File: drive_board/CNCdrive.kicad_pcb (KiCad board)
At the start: 2 copper layers, 1 part, among them U1 DRV8711

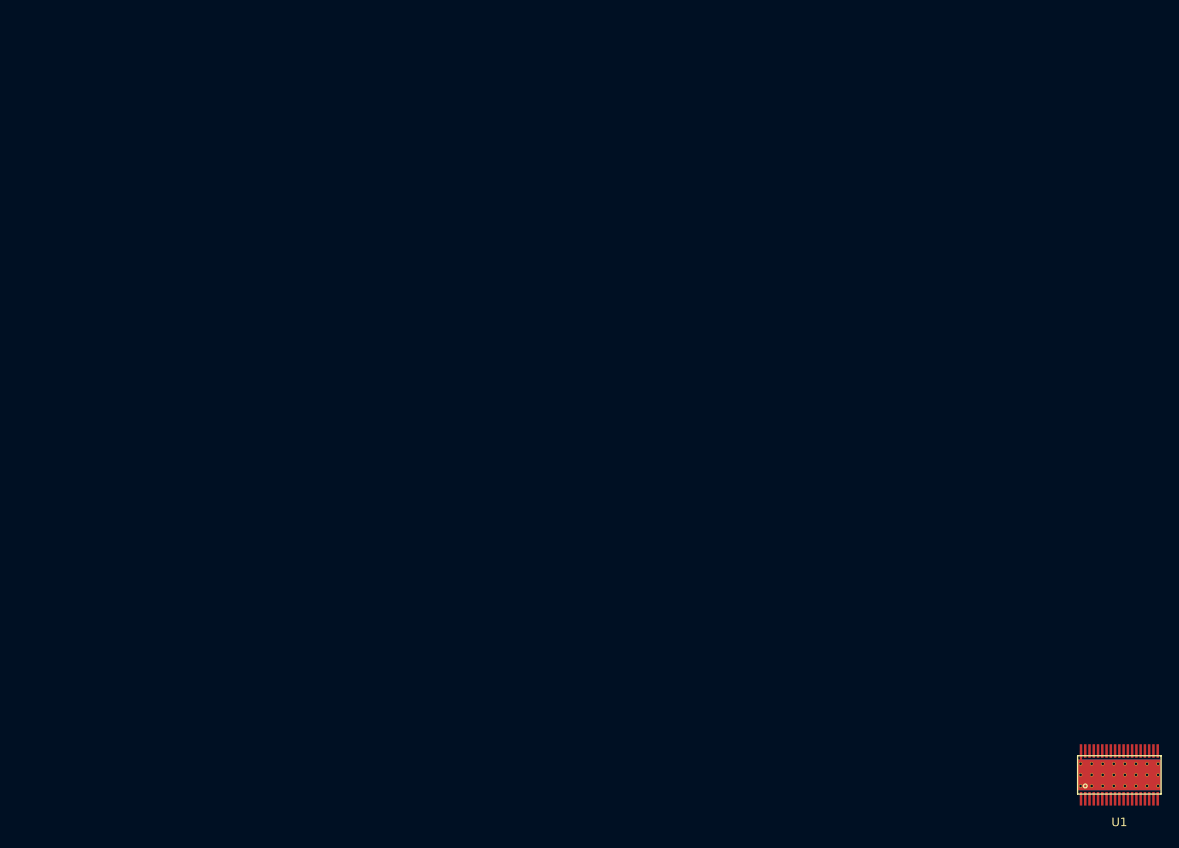
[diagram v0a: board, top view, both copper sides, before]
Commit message: associated footprints, connectors, fuse, leds might need change
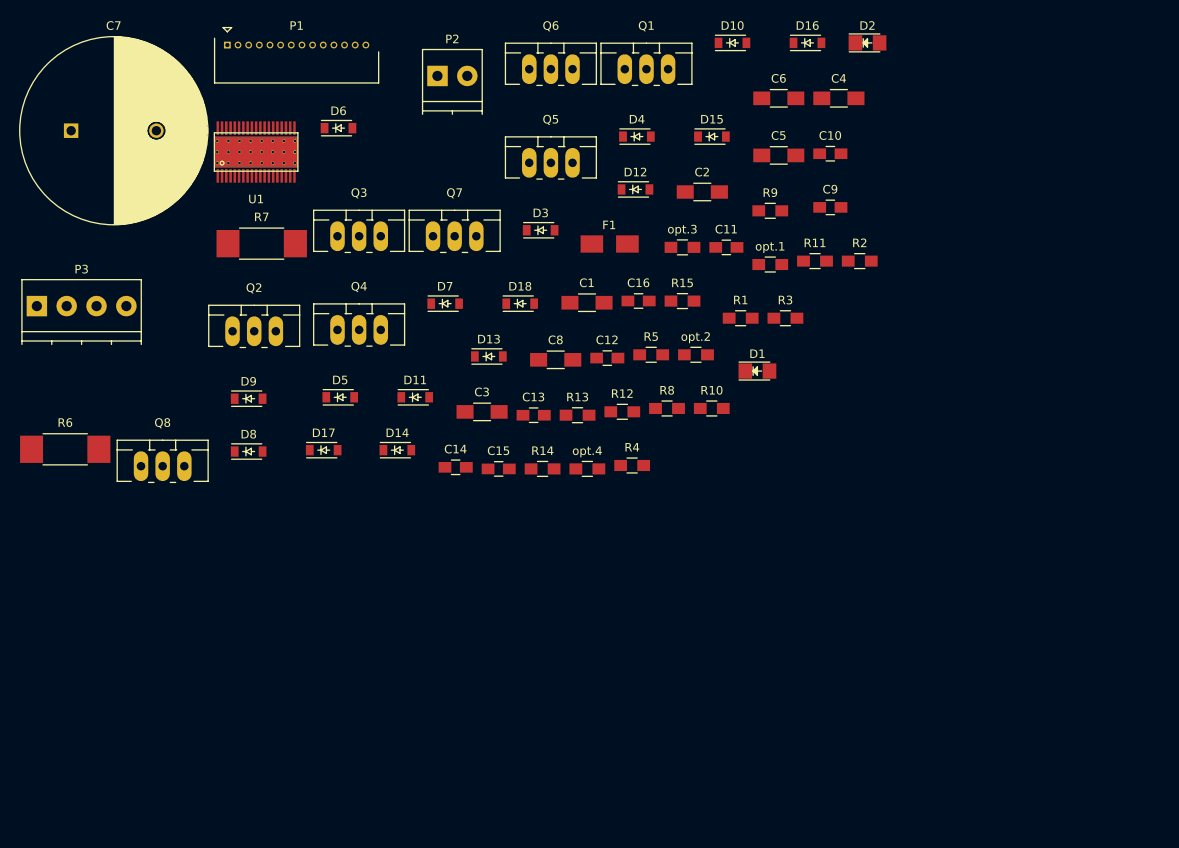
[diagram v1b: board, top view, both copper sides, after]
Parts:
- added C1: 100u, Capacitors_SMD:C_1206_HandSoldering, F.Cu at (86.0, 49.6)
- added C10: snub, Capacitors_SMD:C_0805_HandSoldering, F.Cu at (114.6, 32.1)
- added C11: snub, Capacitors_SMD:C_0805_HandSoldering, F.Cu at (102.4, 43.1)
- added C12: snub, Capacitors_SMD:C_0805_HandSoldering, F.Cu at (88.4, 56.1)
- added C13: snub, Capacitors_SMD:C_0805_HandSoldering, F.Cu at (79.8, 62.8)
- added C14: snub, Capacitors_SMD:C_0805_HandSoldering, F.Cu at (70.6, 68.9)
- added C15: snub, Capacitors_SMD:C_0805_HandSoldering, F.Cu at (75.7, 69.1)
- added C16: snub, Capacitors_SMD:C_0805_HandSoldering, F.Cu at (92.1, 49.4)
- added C2: 10n, Capacitors_SMD:C_1206_HandSoldering, F.Cu at (99.6, 36.6)
- added C3: 100n, Capacitors_SMD:C_1206_HandSoldering, F.Cu at (73.7, 62.4)
- added C4: 1u, Capacitors_SMD:C_1206_HandSoldering, F.Cu at (115.6, 25.6)
- added C5: 1u, Capacitors_SMD:C_1206_HandSoldering, F.Cu at (108.5, 32.3)
- added C6: 100n, Capacitors_SMD:C_1206_HandSoldering, F.Cu at (108.5, 25.6)
- added C7: 1000u, Capacitors_ThroughHole:C_Radial_D22_L41_P10, F.Cu at (25.5, 29.4)
- added C8: 1n, Capacitors_SMD:C_1206_HandSoldering, F.Cu at (82.4, 56.3)
- added C9: snub, Capacitors_SMD:C_0805_HandSoldering, F.Cu at (114.6, 38.4)
- added D1: LED, LEDs:LED_1206, F.Cu at (106.0, 57.6)
- added D10: ZENER opt., Diodes_SMD:SOD-123, F.Cu at (103.1, 19.1)
- added D11: D_Schottky, Diodes_SMD:SOD-123, F.Cu at (65.9, 60.7)
- added D12: D_Schottky, Diodes_SMD:SOD-123, F.Cu at (91.7, 36.3)
- added D13: D_Schottky, Diodes_SMD:SOD-123, F.Cu at (74.5, 55.9)
- added D14: D_Schottky, Diodes_SMD:SOD-123, F.Cu at (63.8, 66.9)
- added D15: D_Schottky, Diodes_SMD:SOD-123, F.Cu at (100.7, 30.1)
- added D16: D_Schottky, Diodes_SMD:SOD-123, F.Cu at (111.9, 19.1)
- added D17: D_Schottky, Diodes_SMD:SOD-123, F.Cu at (55.2, 66.9)
- added D18: D_Schottky, Diodes_SMD:SOD-123, F.Cu at (78.2, 49.7)
- added D2: LED, LEDs:LED_1206, F.Cu at (119.0, 19.1)
- added D3: ZENER opt., Diodes_SMD:SOD-123, F.Cu at (80.6, 41.1)
- added D4: ZENER opt., Diodes_SMD:SOD-123, F.Cu at (91.9, 30.1)
- added D5: ZENER opt., Diodes_SMD:SOD-123, F.Cu at (57.1, 60.7)
- added D6: ZENER opt., Diodes_SMD:SOD-123, F.Cu at (56.9, 29.1)
- added D7: ZENER opt., Diodes_SMD:SOD-123, F.Cu at (69.4, 49.7)
- added D8: ZENER opt., Diodes_SMD:SOD-123, F.Cu at (46.3, 67.1)
- added D9: ZENER opt., Diodes_SMD:SOD-123, F.Cu at (46.3, 60.9)
- added F1: 5A, Fuse_Holders_and_Fuses:Fuse_SMD1206_HandSoldering, F.Cu at (88.7, 42.7)
- added P1: CONN_01X14, Connectors_Molex:Connector_Molex_PicoBlade_53048-1410, F.Cu at (43.9, 19.4)
- added P2: CONN_01X02, Terminal_Blocks:TerminalBlock_Pheonix_PT-3.5mm_2pol, F.Cu at (68.5, 23.0)
- added P3: CONN_01X04, Terminal_Blocks:TerminalBlock_Pheonix_PT-3.5mm_4pol, F.Cu at (21.5, 50.0)
- added Q1: Q_NMOS_GDS, TO_SOT_Packages_THT:TO-220_Neutral123_Vertical_LargePads, F.Cu at (93.0, 22.2)
- added Q2: Q_NMOS_GDS, TO_SOT_Packages_THT:TO-220_Neutral123_Vertical_LargePads, F.Cu at (47.0, 53.0)
- added Q3: Q_NMOS_GDS, TO_SOT_Packages_THT:TO-220_Neutral123_Vertical_LargePads, F.Cu at (59.3, 41.8)
- added Q4: Q_NMOS_GDS, TO_SOT_Packages_THT:TO-220_Neutral123_Vertical_LargePads, F.Cu at (59.3, 52.8)
- added Q5: Q_NMOS_GDS, TO_SOT_Packages_THT:TO-220_Neutral123_Vertical_LargePads, F.Cu at (81.8, 33.2)
- added Q6: Q_NMOS_GDS, TO_SOT_Packages_THT:TO-220_Neutral123_Vertical_LargePads, F.Cu at (81.8, 22.2)
- added Q7: Q_NMOS_GDS, TO_SOT_Packages_THT:TO-220_Neutral123_Vertical_LargePads, F.Cu at (70.5, 41.8)
- added Q8: Q_NMOS_GDS, TO_SOT_Packages_THT:TO-220_Neutral123_Vertical_LargePads, F.Cu at (36.3, 68.8)
- added R1: 24K, Resistors_SMD:R_0805_HandSoldering, F.Cu at (104.1, 51.4)
- added R10: snub, Resistors_SMD:R_0805_HandSoldering, F.Cu at (100.7, 62.0)
- added R11: snub, Resistors_SMD:R_0805_HandSoldering, F.Cu at (112.8, 44.7)
- added R12: snub, Resistors_SMD:R_0805_HandSoldering, F.Cu at (90.2, 62.4)
- added R13: snub, Resistors_SMD:R_0805_HandSoldering, F.Cu at (84.9, 62.8)
- added R14: snub, Resistors_SMD:R_0805_HandSoldering, F.Cu at (80.8, 69.1)
- added R15: snub, Resistors_SMD:R_0805_HandSoldering, F.Cu at (97.2, 49.4)
- added R2: 1K6, Resistors_SMD:R_0805_HandSoldering, F.Cu at (118.0, 44.7)
- added R3: 3K3, Resistors_SMD:R_0805_HandSoldering, F.Cu at (109.3, 51.4)
- added R4: 3K3, Resistors_SMD:R_0805_HandSoldering, F.Cu at (91.3, 68.7)
- added R5: 3K3, Resistors_SMD:R_0805_HandSoldering, F.Cu at (93.6, 55.7)
- added R6: R, Resistors_SMD:R_2512_HandSoldering, F.Cu at (24.8, 66.8)
- added R7: R, Resistors_SMD:R_2512_HandSoldering, F.Cu at (47.9, 42.7)
- added R8: snub, Resistors_SMD:R_0805_HandSoldering, F.Cu at (95.4, 62.0)
- added R9: snub, Resistors_SMD:R_0805_HandSoldering, F.Cu at (107.5, 38.8)
- added opt.1: R, Resistors_SMD:R_0805_HandSoldering, F.Cu at (107.5, 45.1)
- added opt.2: R, Resistors_SMD:R_0805_HandSoldering, F.Cu at (98.8, 55.7)
- added opt.3: R, Resistors_SMD:R_0805_HandSoldering, F.Cu at (97.2, 43.1)
- added opt.4: R, Resistors_SMD:R_0805_HandSoldering, F.Cu at (86.1, 69.1)
- moved U1 124.9 mm to (47.2, 31.9)
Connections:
- U1 pad 10: Net-(U1-Pad10) -> /STEP/AIN1
- U1 pad 11: Net-(U1-Pad11) -> /DIR/AIN2
- U1 pad 12: Net-(U1-Pad12) -> /BIN1
- U1 pad 13: Net-(U1-Pad13) -> /BIN2
- U1 pad 14: Net-(U1-Pad14) -> /SCLK
- U1 pad 15: Net-(U1-Pad15) -> /SDATI
- U1 pad 16: Net-(U1-Pad16) -> /SCS
- U1 pad 17: Net-(U1-Pad17) -> /SDATO
- U1 pad 18: Net-(U1-Pad18) -> /~FAULT
- U1 pad 19: Net-(U1-Pad19) -> /~STALL/BEMFV
- U1 pad 20: Net-(U1-Pad20) -> /BEMF
- U1 pad 24: Net-(U1-Pad24) -> (no net)
- U1 pad 25: Net-(U1-Pad25) -> /BISENP
- U1 pad 29: Net-(U1-Pad29) -> GNDD
- U1 pad 33: Net-(U1-Pad33) -> (no net)
- U1 pad 34: Net-(U1-Pad34) -> /AISENP
- U1 pad 38: Net-(U1-Pad38) -> GNDD
- U1 pad 4: Net-(U1-Pad4) -> +48V
- U1 pad 5: Net-(U1-Pad5) -> GNDD
- U1 pad 6: Net-(U1-Pad6) -> +5V
- U1 pad 8: Net-(U1-Pad8) -> /~SLEEP
- U1 pad 9: Net-(U1-Pad9) -> /RESET
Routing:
- net Net-(U1-Pad38): track 1.52 -> 0.00 mm

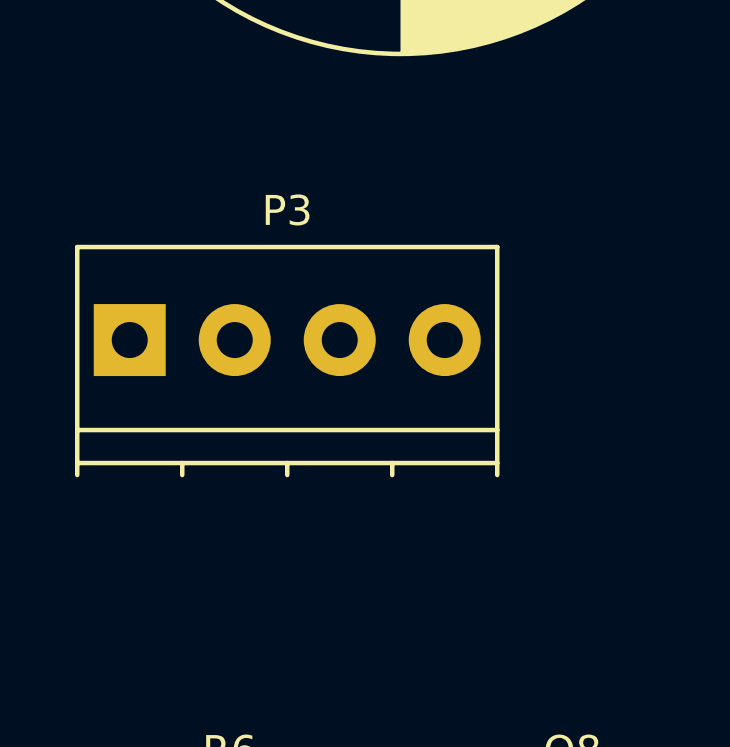
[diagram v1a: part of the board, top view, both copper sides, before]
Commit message: added footprints, leds, fuse , conns may change
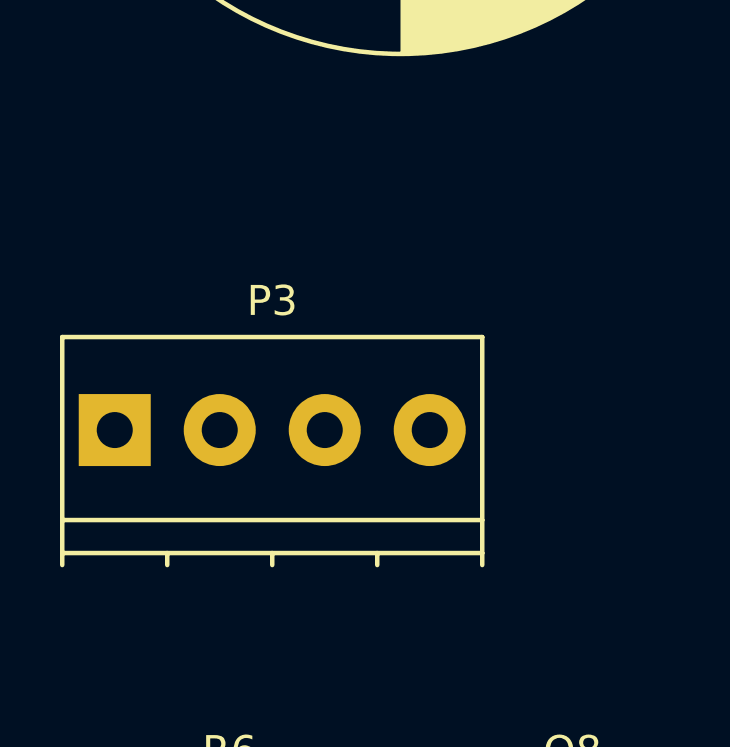
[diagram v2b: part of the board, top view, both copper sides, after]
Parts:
- moved P3 3.04 mm to (21.0, 53.0)
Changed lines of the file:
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@@
     (links 165)
     (no_connects 139)
-    (area 0 0 0 0)
+    (area 19 16 121.680002 73.57)
     (thickness 1.6)
     (drawings 0)
@@
   )
   (module Terminal_Blocks:TerminalBlock_Pheonix_PT-3.5mm_4pol (layer F.Cu)
-    (at 21.5 50)
+    (at 21 53)
     (descr "4-way 3.5mm pitch terminal block, Phoenix PT series")
     (fp_text reference P3 (at 5.25 -4.3) (layer F.SilkS)
